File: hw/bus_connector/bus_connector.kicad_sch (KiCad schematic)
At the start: 10 parts, among them J1 DB9_Top, J2 DB9_Right, J3 DB9_Left

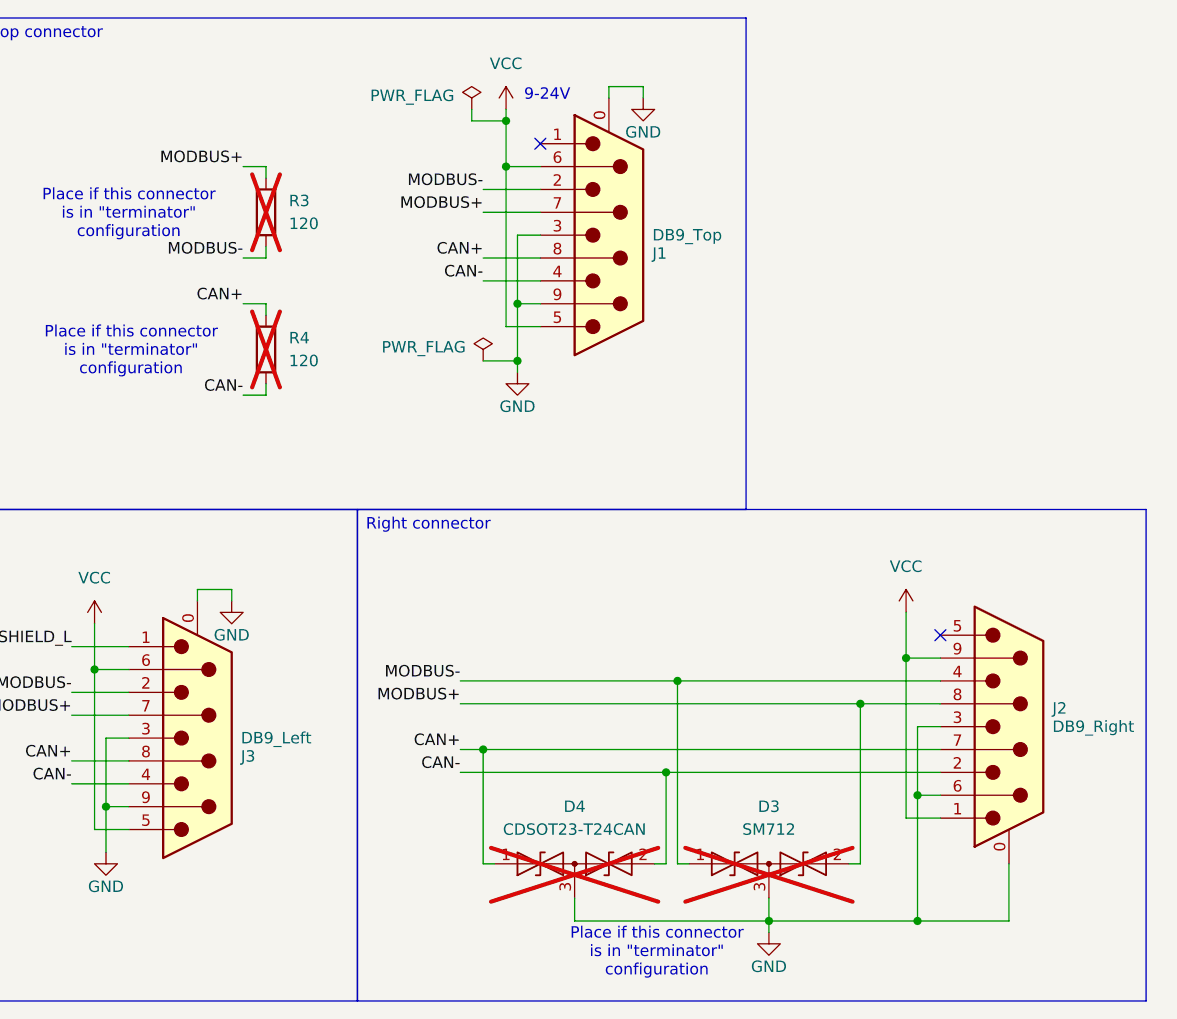
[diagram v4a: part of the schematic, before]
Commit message: Fix silkscreen
Signed-off-by: Mateusz Pająk <22417805+Tai-Min@users.noreply.github.com>
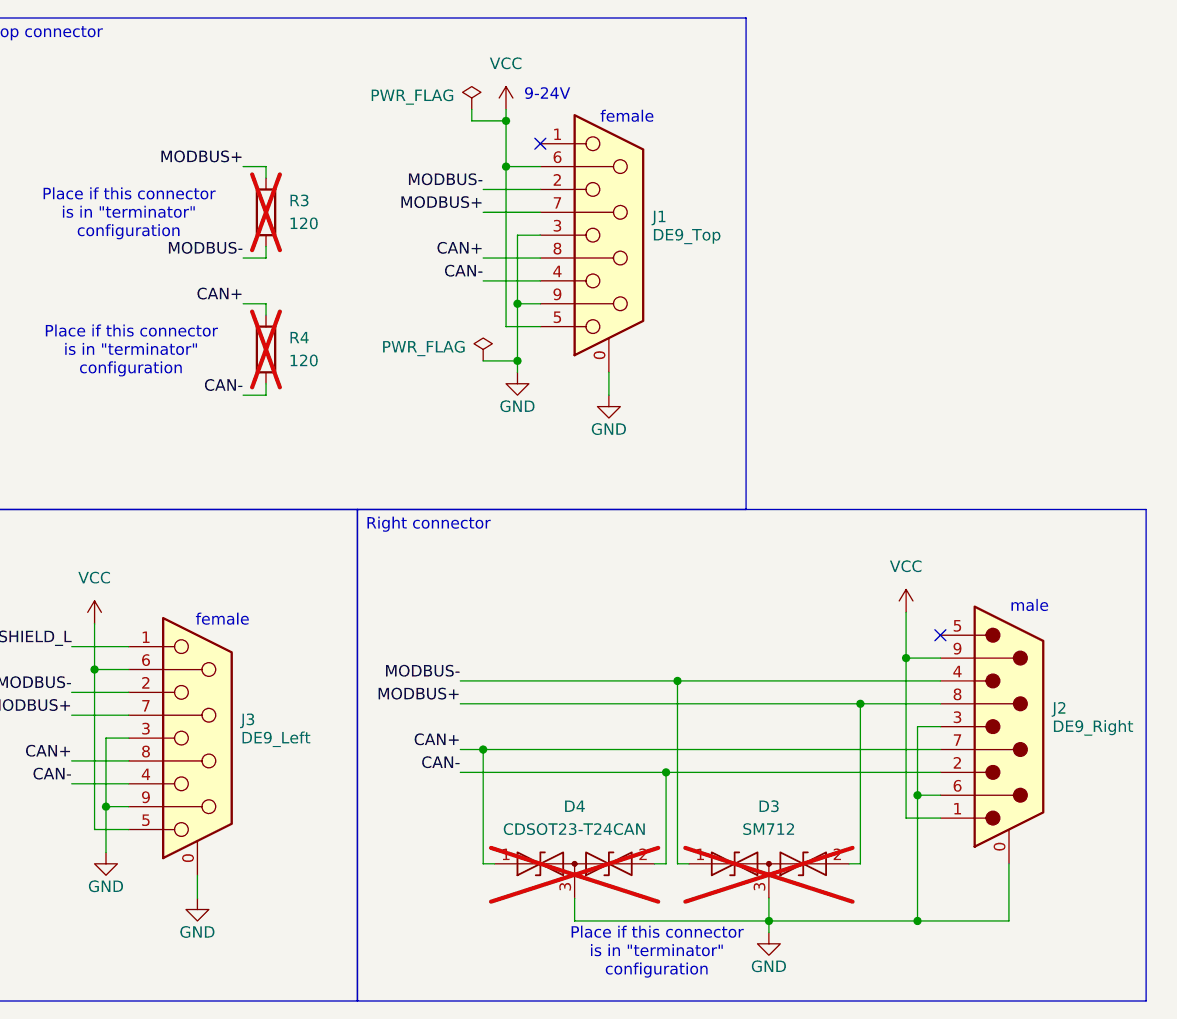
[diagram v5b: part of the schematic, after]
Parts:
- J1: value DB9_Top -> DE9_Top
- J2: value DB9_Right -> DE9_Right
- J3: value DB9_Left -> DE9_Left
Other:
- note added: "female"
- note added: "male"
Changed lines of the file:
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@@
+		)
+	)
+	(text "female"
+		(exclude_from_sim no)
+		(at 137.414 103.886 0)
+		(effects
+			(font
+				(size 1.27 1.27)
+			)
 		)
 	)
@@
 		)
 	)
+	(text "female"
+		(exclude_from_sim no)
+		(at 182.372 48.006 0)
+		(effects
+			(font
+				(size 1.27 1.27)
+			)
+		)
+	)
 	(text "Right connector"
 		(exclude_from_sim no)
@@
 		(exclude_from_sim no)
 		(at 67.056 93.218 0)
+		(effects
+			(font
+				(size 1.27 1.27)
+			)
+		)
+	)
+	(text "male"
+		(exclude_from_sim no)
+		(at 227.076 102.362 0)
 		(effects
 			(font
@@
 	(wire
 		(pts
+			(xy 180.34 76.2) (xy 180.34 78.74)
+		)
+		(stroke
+			(width 0)
+			(type default)
+		)
+	)
+	(wire
+		(pts
 			(xy 127 116.84) (xy 124.46 116.84)
 		)
@@
 	(wire
 		(pts
-			(xy 134.62 100.33) (xy 138.43 100.33)
-		)
-		(stroke
-			(width 0)
-			(type default)
-		)
-	)
-	(wire
-		(pts
-			(xy 180.34 44.45) (xy 184.15 44.45)
-		)
-		(stroke
-			(width 0)
-			(type default)
-		)
-	)
-	(wire
-		(pts
 			(xy 139.7 63.5) (xy 142.24 63.5)
 		)
@@
 	(wire
 		(pts
-			(xy 184.15 44.45) (xy 184.15 45.72)
-		)
-		(stroke
-			(width 0)
-			(type default)
-		)
-	)
-	(wire
-		(pts
 			(xy 124.46 116.84) (xy 124.46 124.46)
 		)
@@
 	(wire
 		(pts
+			(xy 134.62 132.08) (xy 134.62 134.62)
+		)
+		(stroke
+			(width 0)
+			(type default)
+		)
+	)
+	(wire
+		(pts
 			(xy 166.37 118.11) (xy 217.17 118.11)
 		)
@@
 	(wire
 		(pts
-			(xy 180.34 45.72) (xy 180.34 44.45)
-		)
-		(stroke
-			(width 0)
-			(type default)
-		)
-	)
-	(wire
-		(pts
 			(xy 163.83 118.11) (xy 166.37 118.11)
 		)
@@
 	(wire
 		(pts
-			(xy 138.43 100.33) (xy 138.43 101.6)
-		)
-		(stroke
-			(width 0)
-			(type default)
-		)
-	)
-	(wire
-		(pts
 			(xy 186.69 120.65) (xy 186.69 130.81)
 		)
@@
 		(pts
 			(xy 96.52 124.46) (xy 96.52 123.19)
-		)
-		(stroke
-			(width 0)
-			(type default)
-		)
-	)
-	(wire
-		(pts
-			(xy 134.62 101.6) (xy 134.62 100.33)
 		)
 		(stroke
@@
 	(symbol
 		(lib_id "power:GND")
-		(at 138.43 101.6 0)
+		(at 134.62 134.62 0)
 		(unit 1)
 		(exclude_from_sim no)
@@
 		(dnp no)
 		(property "Reference" "#PWR09"
-			(at 138.43 107.95 0)
+			(at 134.62 140.97 0)
 			(effects
 				(font
@@
 		)
 		(property "Value" "GND"
-			(at 138.43 105.41 0)
+			(at 134.62 138.43 0)
 			(effects
 				(font
@@
 		)
 		(property "Footprint" ""
-			(at 138.43 101.6 0)
+			(at 134.62 134.62 0)
 			(effects
 				(font
@@
 		)
 		(property "Datasheet" ""
-			(at 138.43 101.6 0)
+			(at 134.62 134.62 0)
 			(effects
 				(font
@@
 		)
 		(property "Description" "Power symbol creates a global label with name \"GND\" , ground"
-			(at 138.43 101.6 0)
+			(at 134.62 134.62 0)
 			(effects
 				(font
@@
 			)
 		)
-		(property "Value" "DB9_Right"
+		(property "Value" "DE9_Right"
 			(at 229.616 115.57 0)
 			(effects
@@
 	(symbol
 		(lib_id "power:GND")
-		(at 184.15 45.72 0)
+		(at 180.34 78.74 0)
 		(unit 1)
 		(exclude_from_sim no)
@@
 		(dnp no)
 		(property "Reference" "#PWR04"
-			(at 184.15 52.07 0)
+			(at 180.34 85.09 0)
 			(effects
 				(font
@@
 		)
 		(property "Value" "GND"
-			(at 184.15 49.53 0)
+			(at 180.34 82.55 0)
 			(effects
 				(font
@@
 		)
 		(property "Footprint" ""
-			(at 184.15 45.72 0)
+			(at 180.34 78.74 0)
 			(effects
 				(font
@@
 		)
 		(property "Datasheet" ""
-			(at 184.15 45.72 0)
+			(at 180.34 78.74 0)
 			(effects
 				(font
@@
 		)
 		(property "Description" "Power symbol creates a global label with name \"GND\" , ground"
-			(at 184.15 45.72 0)
+			(at 180.34 78.74 0)
 			(effects
 				(font
@@
 	)
 	(symbol
+		(lib_name "DE9_Pins_MountingHoles_1")
 		(lib_id "Connector:DE9_Pins_MountingHoles")
 		(at 134.62 116.84 0)
-		(mirror x)
 		(unit 1)
 		(exclude_from_sim no)
@@
 		(dnp no)
 		(property "Reference" "J3"
-			(at 139.446 118.872 0)
+			(at 139.446 114.808 0)
 			(effects
 				(font
@@
 			)
 		)
-		(property "Value" "DB9_Left"
+		(property "Value" "DE9_Left"
 			(at 139.446 116.84 0)
 			(effects
@@
 		)
 		(property "Footprint" "Connector_Dsub:DSUB-9_Pins_Horizontal_P2.77x2.84mm_EdgePinOffset7.70mm_Housed_MountingHolesOffset9.12mm"
-			(at 134.62 116.84 0)
+			(at 139.446 116.078 90)
 			(effects
 				(font
@@
 		)
 		(property "Description" "9-pin D-SUB connector, pins (male), Mounting Hole"
-			(at 134.62 116.84 0)
+			(at 139.446 116.84 90)
 			(effects
 				(font
@@
 	)
 	(symbol
+		(lib_name "DE9_Pins_MountingHoles_2")
 		(lib_id "Connector:DE9_Pins_MountingHoles")
 		(at 180.34 60.96 0)
-		(mirror x)
 		(unit 1)
 		(exclude_from_sim no)
@@
 		(dnp no)
 		(property "Reference" "J1"
-			(at 185.166 62.992 0)
+			(at 185.166 58.928 0)
 			(effects
 				(font
@@
 			)
 		)
-		(property "Value" "DB9_Top"
+		(property "Value" "DE9_Top"
 			(at 185.166 60.96 0)
 			(effects
@@
 		)
 		(property "Footprint" "Connector_Dsub:DSUB-9_Pins_Horizontal_P2.77x2.84mm_EdgePinOffset7.70mm_Housed_MountingHolesOffset9.12mm"
-			(at 180.34 60.96 0)
+			(at 185.674 60.706 90)
 			(effects
 				(font
@@
 		)
 		(property "Description" "9-pin D-SUB connector, pins (male), Mounting Hole"
-			(at 180.34 60.96 0)
-			(effects
-				(font
+			(at 185.674 60.96 90)
+			(effects
+				(font

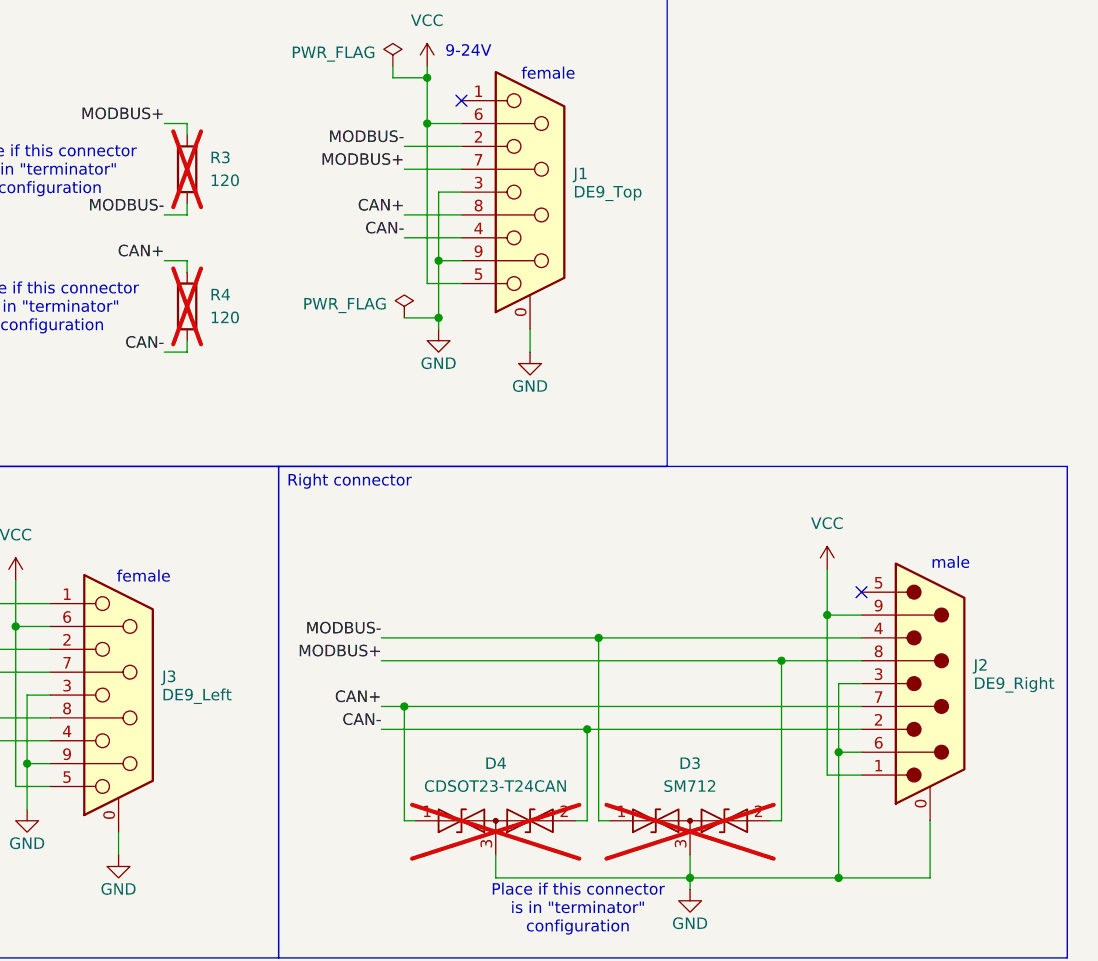
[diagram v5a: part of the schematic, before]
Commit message: Add datasheets, minor pcb changes
Signed-off-by: Mateusz Pająk <22417805+Tai-Min@users.noreply.github.com>
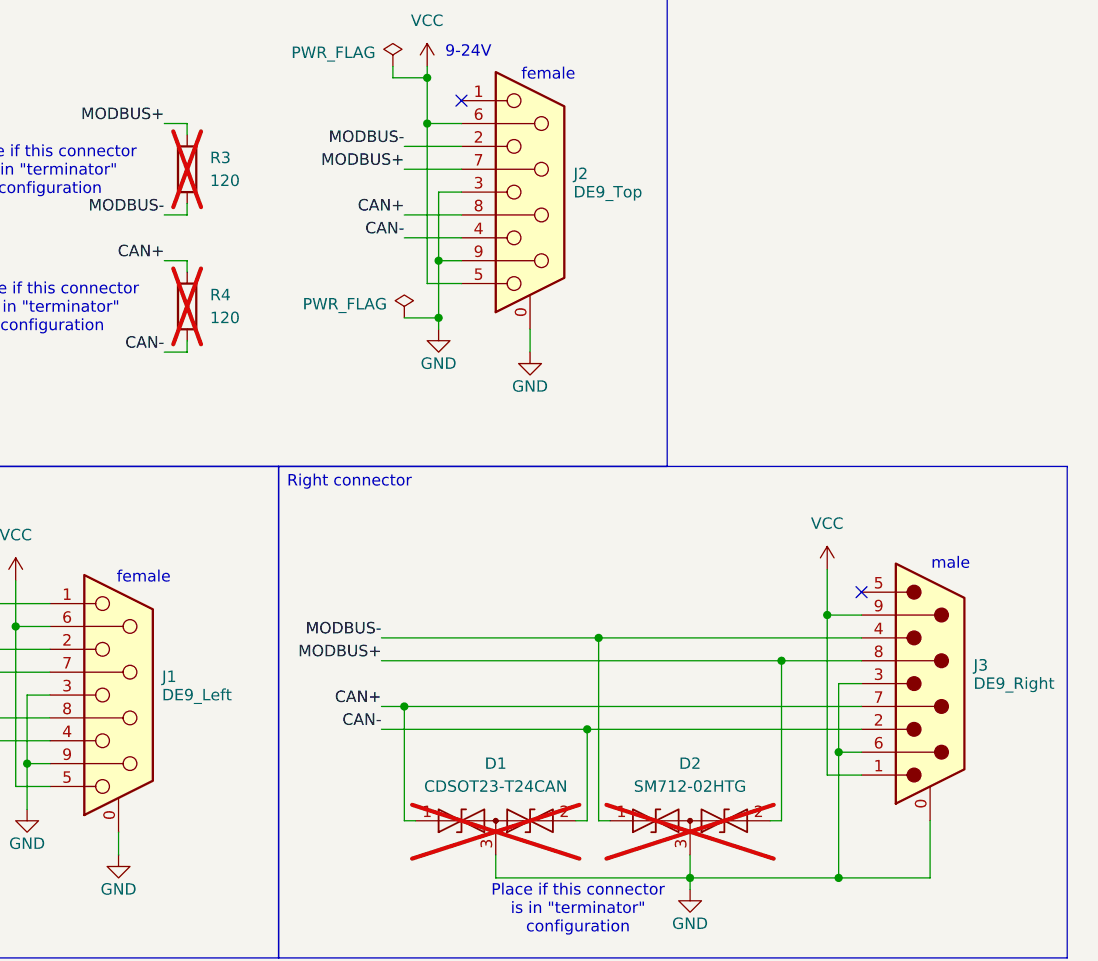
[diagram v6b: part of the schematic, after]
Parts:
- D1: renamed from D4; LCSC (none) -> https://www.lcsc.com/product-detail/C2959841.html?s_z=n_CDS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
- D2: renamed from D3; value SM712 -> SM712-02HTG; LCSC (none) -> https://www.lcsc.com/product-detail/C172881.html?s_z=n_SM712
- J1: renamed from J3; LCSC (none) -> https://www.lcsc.com/product-detail/C19077337.html?s_z=n_XU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
- J2: renamed from J1; LCSC (none) -> https://www.lcsc.com/product-detail/C19077337.html?s_z=n_XU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
- J3: renamed from J2; LCSC (none) -> https://www.lcsc.com/product-detail/C19077344.html?s_z=n_ds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
- R1, R2, R3, R4: LCSC (none) -> https://www.lcsc.com/product-detail/C114928.html
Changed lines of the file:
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@@
 		(on_board yes)
 		(dnp no)
-		(property "Reference" "#PWR08"
+		(property "Reference" "#PWR03"
 			(at 124.46 135.89 0)
 			(effects
@@
 			(project "terminator"
 				(path "/e42bcc36-c7d3-414a-8e1a-42e6cdd67034"
-					(reference "#PWR08")
+					(reference "#PWR03")
 					(unit 1)
 				)
@@
 			)
 		)
+		(property "LCSC" "https://www.lcsc.com/product-detail/C114928.html"
+			(at 96.52 119.38 0)
+			(effects
+				(font
+					(size 1.27 1.27)
+				)
+				(hide yes)
+			)
+		)
 		(pin "1"
 		)
@@
 		(on_board yes)
 		(dnp no)
-		(property "Reference" "#PWR09"
+		(property "Reference" "#PWR04"
 			(at 134.62 140.97 0)
 			(effects
@@
 			(project "terminator"
 				(path "/e42bcc36-c7d3-414a-8e1a-42e6cdd67034"
-					(reference "#PWR09")
+					(reference "#PWR04")
 					(unit 1)
 				)
@@
 		(on_board yes)
 		(dnp no)
-		(property "Reference" "J2"
+		(property "Reference" "J3"
 			(at 229.616 113.538 0)
 			(effects
@@
 			)
 		)
-		(property "Datasheet" "~"
+		(property "Datasheet" "\\datasheets\\de9_male.pdf"
 			(at 224.79 115.57 0)
 			(effects
@@
 			)
 		)
+		(property "LCSC" "https://www.lcsc.com/product-detail/C19077344.html?s_z=n_dsub"
+			(at 224.79 115.57 0)
+			(effects
+				(font
+					(size 1.27 1.27)
+				)
+				(hide yes)
+			)
+		)
 		(pin "7"
 		)
@@
 			(project "terminator"
 				(path "/e42bcc36-c7d3-414a-8e1a-42e6cdd67034"
-					(reference "J2")
+					(reference "J3")
 					(unit 1)
 				)
@@
 			)
 		)
+		(property "LCSC" "https://www.lcsc.com/product-detail/C114928.html"
+			(at 142.24 58.42 0)
+			(effects
+				(font
+					(size 1.27 1.27)
+				)
+				(hide yes)
+			)
+		)
 		(pin "1"
 		)
@@
 			)
 		)
+		(property "LCSC" "https://www.lcsc.com/product-detail/C114928.html"
+			(at 142.24 73.66 0)
+			(effects
+				(font
+					(size 1.27 1.27)
+				)
+				(hide yes)
+			)
+		)
 		(pin "1"
 		)
@@
 		(dnp no)
 		(fields_autoplaced yes)
-		(property "Reference" "#PWR012"
+		(property "Reference" "#PWR05"
 			(at 168.91 50.8 0)
 			(effects
@@
 			(project ""
 				(path "/e42bcc36-c7d3-414a-8e1a-42e6cdd67034"
-					(reference "#PWR012")
+					(reference "#PWR05")
 					(unit 1)
 				)
@@
 		(dnp no)
 		(fields_autoplaced yes)
-		(property "Reference" "#PWR010"
+		(property "Reference" "#PWR09"
 			(at 213.36 106.68 0)
 			(effects
@@
 			(project "bus_connector"
 				(path "/e42bcc36-c7d3-414a-8e1a-42e6cdd67034"
-					(reference "#PWR010")
+					(reference "#PWR09")
 					(unit 1)
 				)
@@
 			)
 		)
+		(property "LCSC" "https://www.lcsc.com/product-detail/C114928.html"
+			(at 96.52 104.14 0)
+			(effects
+				(font
+					(size 1.27 1.27)
+				)
+				(hide yes)
+			)
+		)
 		(pin "1"
 		)
@@
 		(on_board yes)
 		(dnp no)
-		(property "Reference" "#PWR04"
+		(property "Reference" "#PWR07"
 			(at 180.34 85.09 0)
 			(effects
@@
 			(project "terminator"
 				(path "/e42bcc36-c7d3-414a-8e1a-42e6cdd67034"
-					(reference "#PWR04")
+					(reference "#PWR07")
 					(unit 1)
 				)
@@
 		(on_board yes)
 		(dnp no)
-		(property "Reference" "#PWR07"
+		(property "Reference" "#PWR08"
 			(at 198.12 144.78 0)
 			(effects
@@
 			(project "bus_connector"
 				(path "/e42bcc36-c7d3-414a-8e1a-42e6cdd67034"
-					(reference "#PWR07")
+					(reference "#PWR08")
 					(unit 1)
 				)
@@
 		(dnp yes)
 		(fields_autoplaced yes)
-		(property "Reference" "D3"
+		(property "Reference" "D2"
 			(at 198.12 124.46 0)
 			(effects
@@
 			)
 		)
-		(property "Value" "SM712"
+		(property "Value" "SM712-02HTG"
 			(at 198.12 127 0)
 			(effects
@@
 			)
 		)
-		(property "Datasheet" "https://www.littelfuse.com/~/media/electronics/datasheets/tvs_diode_arrays/littelfuse_tvs_diode_array_sm712_datasheet.pdf.pdf"
+		(property "Datasheet" "\\datasheets\\SM712-02HTG.pdf"
 			(at 194.31 130.81 0)
 			(effects
@@
 			)
 		)
+		(property "LCSC" "https://www.lcsc.com/product-detail/C172881.html?s_z=n_SM712"
+			(at 198.12 130.81 0)
+			(effects
+				(font
+					(size 1.27 1.27)
+				)
+				(hide yes)
+			)
+		)
 		(pin "2"
 		)
@@
 			(project "bus_connector"
 				(path "/e42bcc36-c7d3-414a-8e1a-42e6cdd67034"
-					(reference "D3")
+					(reference "D2")
 					(unit 1)
 				)
@@
 		(dnp yes)
 		(fields_autoplaced yes)
-		(property "Reference" "D4"
+		(property "Reference" "D1"
 			(at 176.53 124.46 0)
 			(effects
@@
 			)
 		)
-		(property "Datasheet" ""
+		(property "Datasheet" "\\datasheets\\CDSOT23-T24CAN.pdf"
 			(at 172.72 130.81 0)
 			(effects
@@
 			)
 		)
+		(property "LCSC" "https://www.lcsc.com/product-detail/C2959841.html?s_z=n_CDSOT23-T24CAN"
+			(at 176.53 130.81 0)
+			(effects
+				(font
+					(size 1.27 1.27)
+				)
+				(hide yes)
+			)
+		)
 		(pin "2"
 		)
@@
 			(project "bus_connector"
 				(path "/e42bcc36-c7d3-414a-8e1a-42e6cdd67034"
-					(reference "D4")
+					(reference "D1")
 					(unit 1)
 				)
@@
 		(on_board yes)
 		(dnp no)
-		(property "Reference" "J3"
+		(property "Reference" "J1"
 			(at 139.446 114.808 0)
 			(effects
@@
 			)
 		)
-		(property "Datasheet" "~"
+		(property "Datasheet" "\\datasheets\\de9_female.pdf"
 			(at 134.62 116.84 0)
 			(effects
@@
 			)
 		)
+		(property "LCSC" "https://www.lcsc.com/product-detail/C19077337.html?s_z=n_XUNPU%2520D-SUB-DR-9"
+			(at 134.62 116.84 0)
+			(effects
+				(font
+					(size 1.27 1.27)
+				)
+				(hide yes)
+			)
+		)
 		(pin "7"
 		)
@@
 			(project "terminator"
 				(path "/e42bcc36-c7d3-414a-8e1a-42e6cdd67034"
-					(reference "J3")
+					(reference "J1")
 					(unit 1)
 				)
@@
 		(on_board yes)
 		(dnp no)
-		(property "Reference" "#PWR03"
+		(property "Reference" "#PWR06"
 			(at 170.18 82.55 0)
 			(effects
@@
 			(project "terminator"
 				(path "/e42bcc36-c7d3-414a-8e1a-42e6cdd67034"
-					(reference "#PWR03")
+					(reference "#PWR06")
 					(unit 1)
 				)
@@
 		(on_board yes)
 		(dnp no)
-		(property "Reference" "J1"
+		(property "Reference" "J2"
 			(at 185.166 58.928 0)
 			(effects
@@
 			)
 		)
-		(property "Datasheet" "~"
+		(property "Datasheet" "\\datasheets\\de9_female.pdf"
 			(at 180.34 60.96 0)
 			(effects
@@
 			)
 		)
+		(property "LCSC" "https://www.lcsc.com/product-detail/C19077337.html?s_z=n_XUNPU%2520D-SUB-DR-9"
+			(at 180.34 60.96 0)
+			(effects
+				(font
+					(size 1.27 1.27)
+				)
+				(hide yes)
+			)
+		)
 		(pin "7"
 		)
@@
 			(project "terminator"
 				(path "/e42bcc36-c7d3-414a-8e1a-42e6cdd67034"
-					(reference "J1")
-					(unit 1)
-				)
+					(reference "J2")
+					(unit 1)
+				)
